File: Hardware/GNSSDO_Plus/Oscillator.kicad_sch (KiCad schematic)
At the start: 22 parts, among them U13 STP3593LF, U19 PCA9306

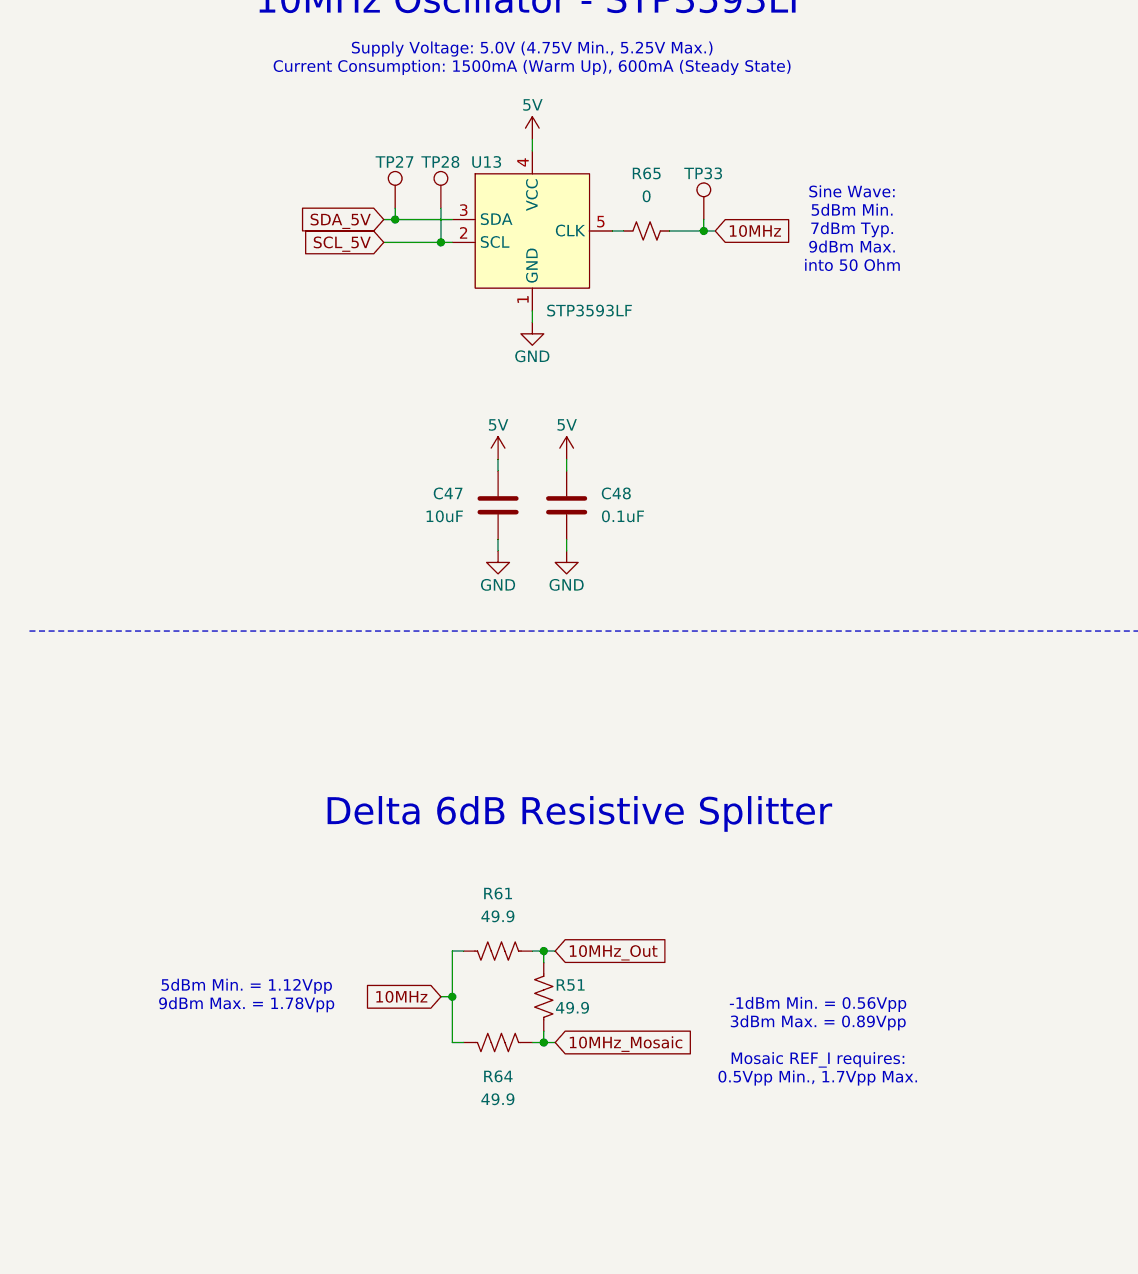
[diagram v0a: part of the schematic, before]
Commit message: GNSSDO Plus: add 3-way splitter
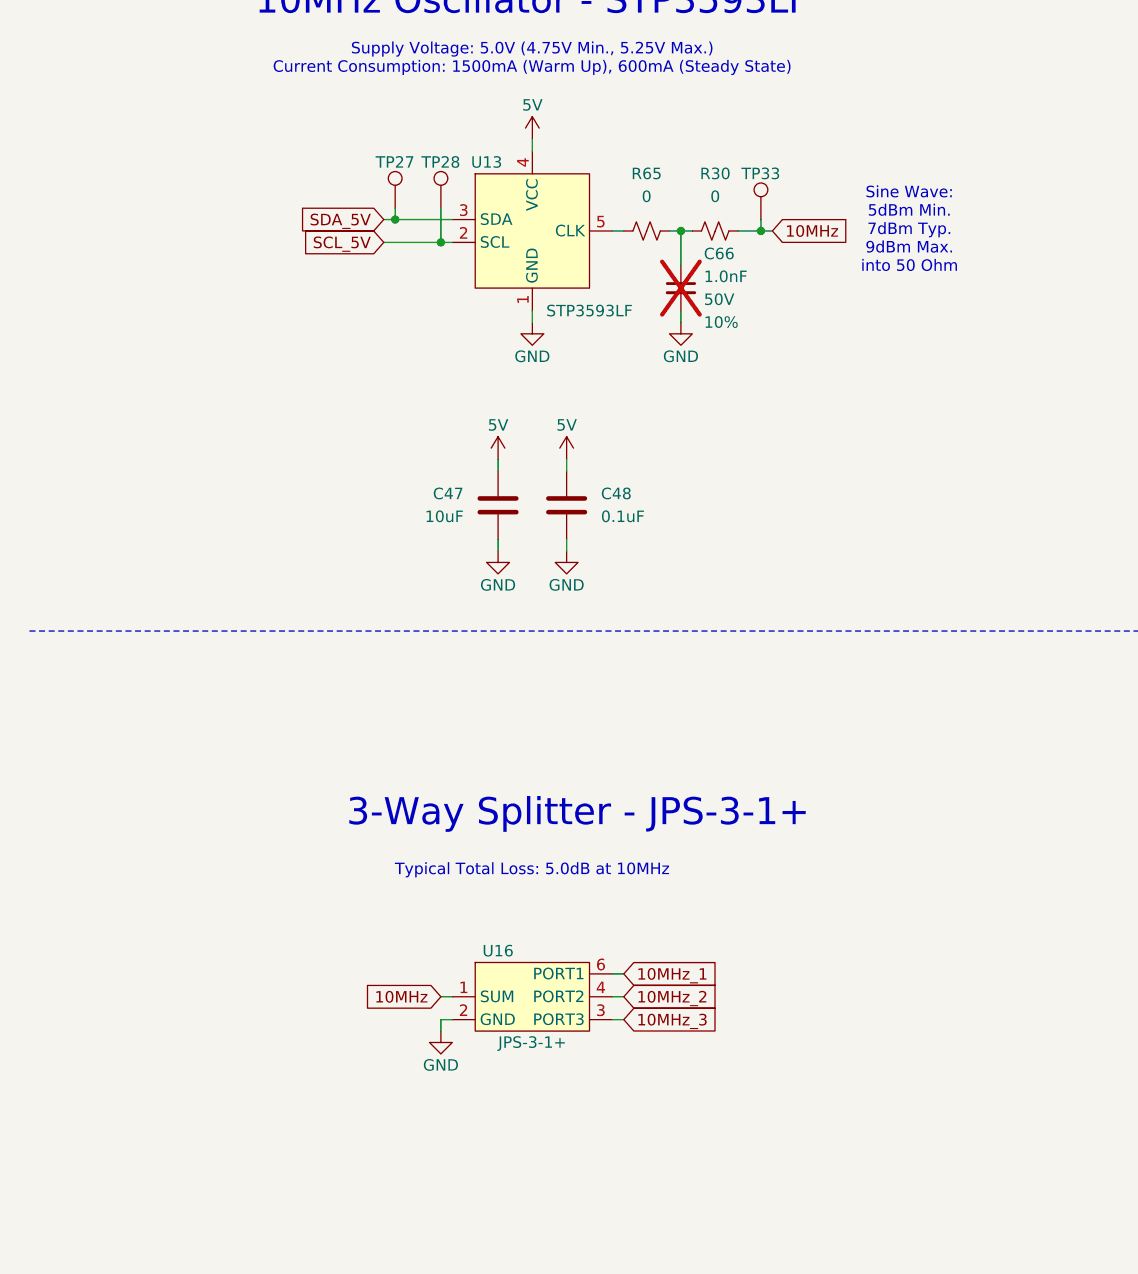
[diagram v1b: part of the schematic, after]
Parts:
- removed R51, R61, R64: 49.9, SparkFun-Resistor:R_0603_1608Metric, symbol SparkFun-Resistor:49.9_0603
- added C66: 1.0nF, SparkFun-Capacitor:C_0603_1608Metric, symbol SparkFun-Capacitor:1.0nF_0603_50V_10%
- added R30: 0, SparkFun-Resistor:R_0603_1608Metric, symbol SparkFun-Resistor:0_0603
- added U16: JPS-3-1+, SparkFun-RF:Mini-Circuits_BH292, symbol SparkFun-RF:Power_Splitter_JPS-3-1+
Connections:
- net 10MHz: now also R30.2, U16.1 (SUM); no longer R65.2
- net GND: now also C66.2, U16.2 (GND), U16.5 (GND)
- new net: C66.1, R30.1, R65.2
- new net 10MHz_1: U16.6 (PORT1)
- new net 10MHz_2: U16.4 (PORT2)
- new net 10MHz_3: U16.3 (PORT3)
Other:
- note added: "3-Way Splitter - JPS-3-1+"
- note added: "Typical Total Loss: 5.0dB at 10MHz"
- note removed: "-1dBm Min. = 0.56Vpp 3dBm Max. = 0.89Vpp Mosaic REF_I requires: 0.5Vpp Min., 1.7Vpp Max."
- note removed: "5dBm Min. = 1.12Vpp 9dBm Max. = 1.78Vpp"
- note removed: "Delta 6dB Resistive Splitter"
- moved on the sheet: TP33

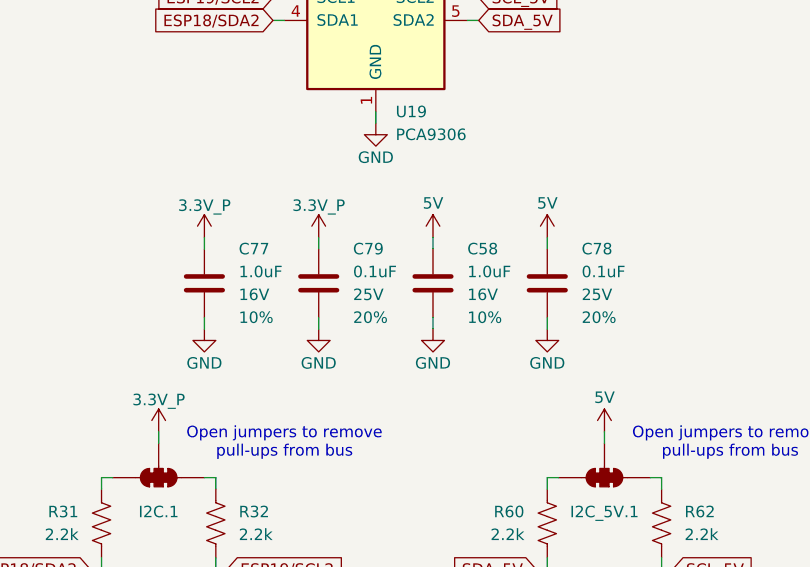
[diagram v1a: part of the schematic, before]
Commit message: GNSSDO+ routed
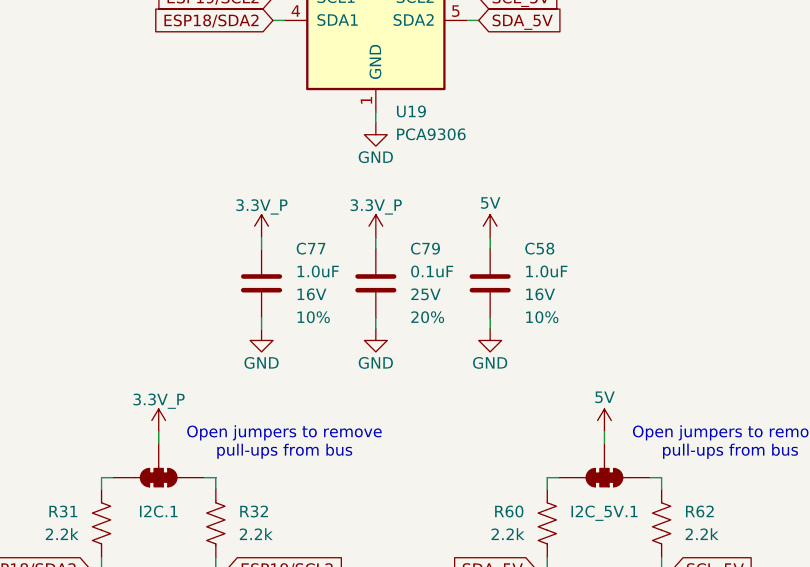
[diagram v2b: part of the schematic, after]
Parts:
- removed C78: 0.1uF, SparkFun-Capacitor:C_0603_1608Metric, symbol SparkFun-Capacitor:0.1uF_0603_25V_20%
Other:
- moved on the sheet: C58, C77, C79

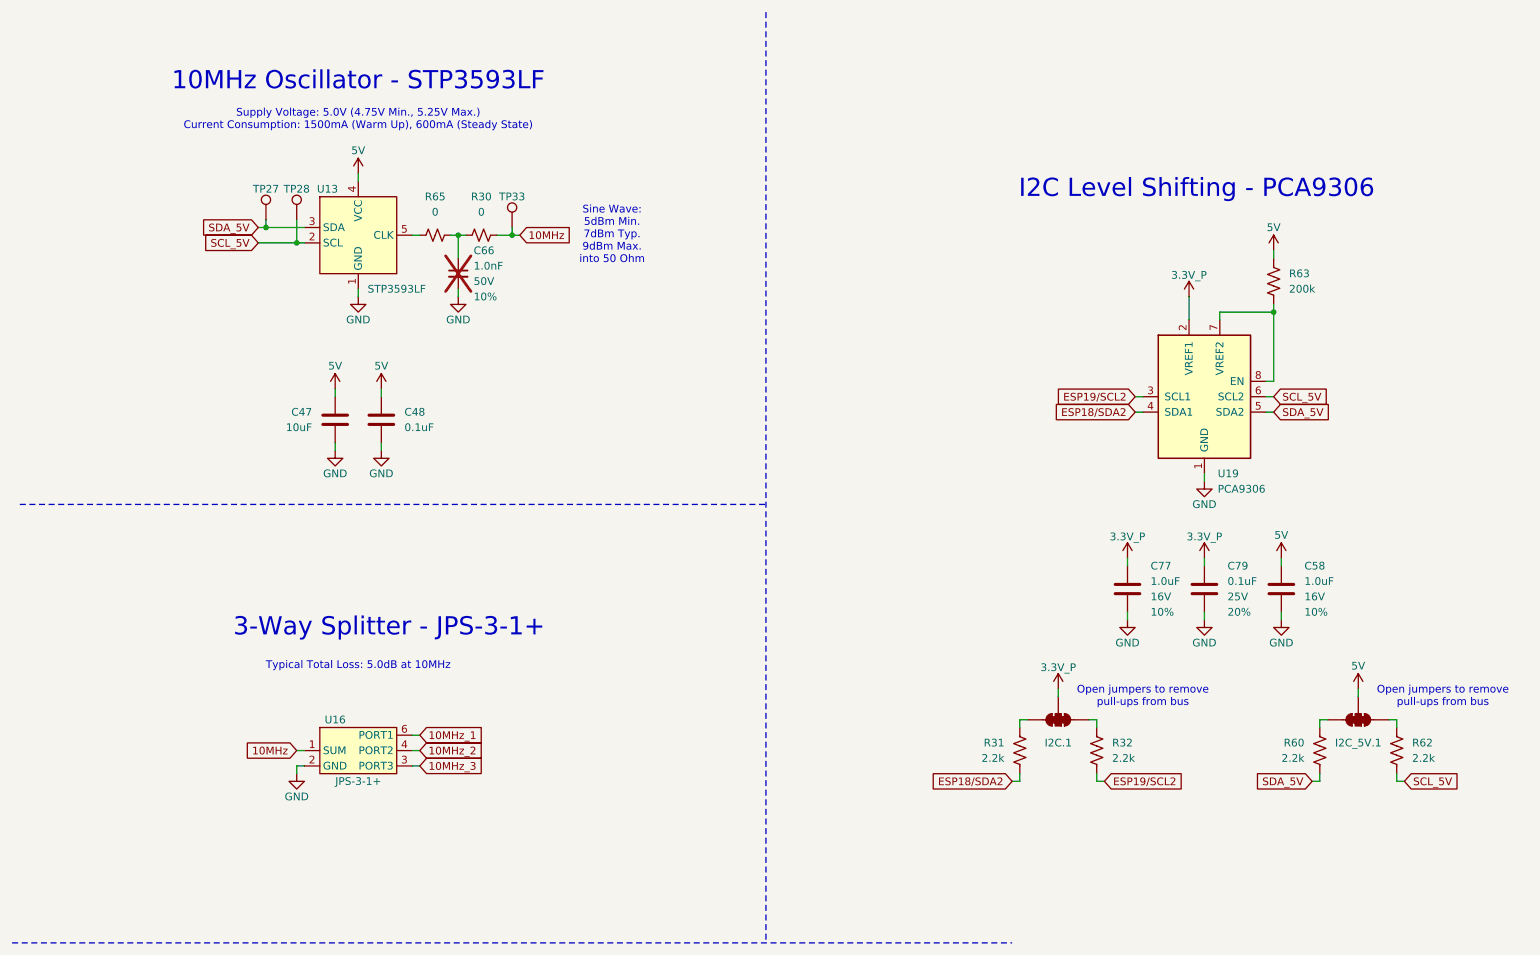
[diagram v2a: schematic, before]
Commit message: GNSSDO+ : update symbols and footprints
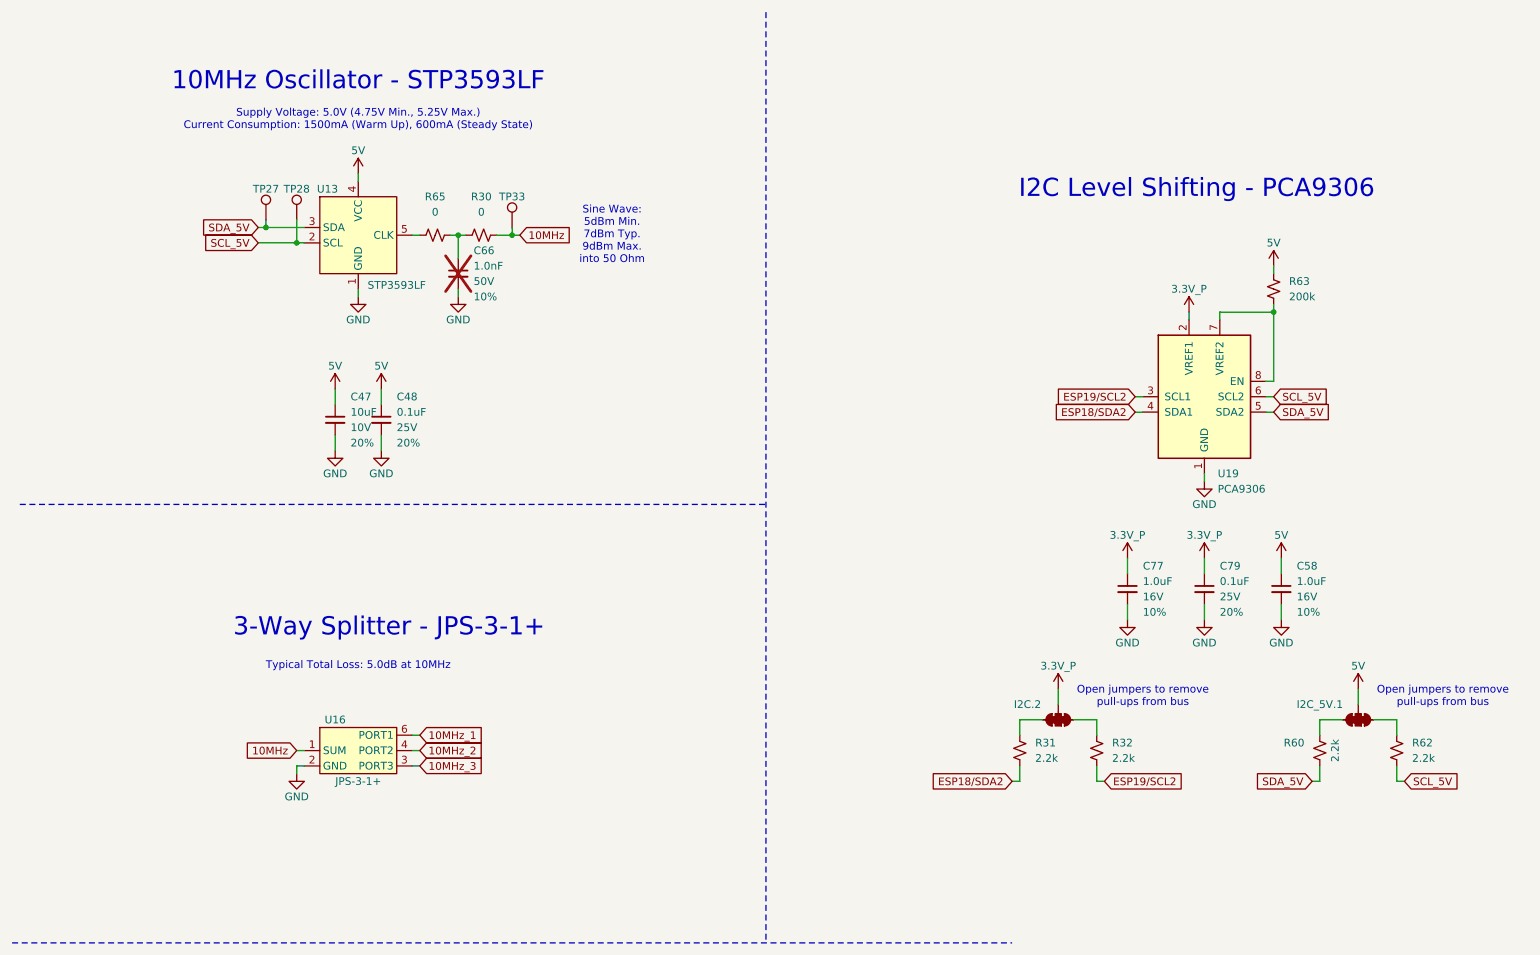
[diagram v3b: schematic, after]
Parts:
- C66: now in the parts list
- U16: PROD_ID (none) -> COMP-24906
- renumbered I2C.1 to I2C.2
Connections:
- net 5V: now also R63.1; no longer R63.2
- net ESP18/SDA2: now also R31.1; no longer R31.2
- net ESP19/SCL2: now also R32.1; no longer R32.2
- net SCL_5V: now also R62.2; no longer R62.1
- net SDA_5V: now also R60.2; no longer R60.1
- net at U19.7 (VREF2), U19.8 (EN): now also R63.2; no longer R63.1
- net at I2C.2.3 (C): now also R31.2; no longer R31.1
- net at I2C_5V.1.1 (A): now also R62.1; no longer R62.2
- net at I2C.2.1 (A): now also R32.2; no longer R32.1
- net at I2C_5V.1.3 (C): now also R60.1; no longer R60.2
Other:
- moved on the sheet: I2C.2, I2C_5V.1

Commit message: GNSSDO Plus - ready for review
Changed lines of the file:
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@@
 		(fields_autoplaced yes)
 		(property "Reference" "C47"
-			(at 67.31 76.2062 0)
+			(at 62.23 76.2062 0)
 			(effects
 				(font
 					(size 1.27 1.27)
 				)
-				(justify right)
+				(justify left)
 			)
 		)
 		(property "Value" "10uF"
-			(at 67.31 78.7462 0)
+			(at 62.23 78.7462 0)
 			(effects
 				(font
 					(size 1.27 1.27)
 				)
-				(justify right)
+				(justify left)
 			)
 		)
@@
 		)
 		(property "Voltage" "10V"
-			(at 67.31 81.2862 0)
+			(at 62.23 81.2862 0)
 			(effects
 				(font
 					(size 1.27 1.27)
 				)
-				(justify right)
+				(justify left)
 			)
 		)
 		(property "Tolerance" "20%"
-			(at 67.31 83.8262 0)
+			(at 62.23 83.8262 0)
 			(effects
 				(font
 					(size 1.27 1.27)
 				)
-				(justify right)
+				(justify left)
 			)
 		)

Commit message: GNSSDO+ v02 PCB - with DP5305 PoE module, PowerPath Controllers and MS8607 PHT sensor
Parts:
- renumbered I2C.2 to JP22, I2C_5V.1 to JP23
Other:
- note added: "I²C Level Shifting - PCA9306"
- note removed: "I2C Level Shifting - PCA9306"
- title: Oscillator -> GNSSDO Plus - Oscillator

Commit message: Update GNSSDO KiCad files to match latest SparkFun library
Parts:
- TP27, TP28, TP33: footprint SparkFun-Connector:1x01 -> SparkFun-Connector:1x01_P2.54mm
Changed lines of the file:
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@@
 		)
 		(instances
-			(project ""
+			(project "SparkPNT_GNSSDO_Plus"
 				(path "/e3dd3ae4-244d-4cba-9cca-5d2abf83f29a/3c582527-c744-4af3-97cb-1f5f96664f58"
 					(reference "C66")
@@
 			)
 		)
-		(property "Footprint" "SparkFun-Connector:1x01"
+		(property "Footprint" "SparkFun-Connector:1x01_P2.54mm"
 			(at 92.71 54.61 0)
 			(effects
@@
 		)
 		(instances
-			(project ""
+			(project "SparkPNT_GNSSDO_Plus"
 				(path "/e3dd3ae4-244d-4cba-9cca-5d2abf83f29a/3c582527-c744-4af3-97cb-1f5f96664f58"
 					(reference "U13")
@@
 		)
 		(instances
-			(project ""
+			(project "SparkPNT_GNSSDO_Plus"
 				(path "/e3dd3ae4-244d-4cba-9cca-5d2abf83f29a/3c582527-c744-4af3-97cb-1f5f96664f58"
 					(reference "R65")
@@
 		)
 		(instances
-			(project ""
+			(project "SparkPNT_GNSSDO_Plus"
 				(path "/e3dd3ae4-244d-4cba-9cca-5d2abf83f29a/3c582527-c744-4af3-97cb-1f5f96664f58"
 					(reference "U16")
@@
 			)
 		)
-		(property "Footprint" "SparkFun-Connector:1x01"
+		(property "Footprint" "SparkFun-Connector:1x01_P2.54mm"
 			(at 57.15 53.34 0)
 			(effects
@@
 			)
 		)
-		(property "Footprint" "SparkFun-Connector:1x01"
+		(property "Footprint" "SparkFun-Connector:1x01_P2.54mm"
 			(at 52.07 53.34 0)
 			(effects
